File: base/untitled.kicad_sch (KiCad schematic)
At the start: 56 parts, among them U23 6N137, U24 6N137, U25 6N137, U26 6N137, U27 6N137, U28 6N137, U29 6N137, U30 6N137, U31 6N137, U32 6N137, U33 6N137, U34 6N137, U36 6N137, U37 6N137

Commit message: changes to schematic
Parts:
- removed C20, C21, C22, C23, C24, C25, C26, C27, C28, C29, C30, C31, C35, C36: 0.1µ, symbol Device:C
- removed R46, R47, R48, R49, R54, R55, R56, R57, R62, R63, R64, R65, R71, R72: R, symbol Device:R
- removed R50, R51, R52, R53, R58, R59, R60, R61, R66, R67, R68, R69, R73, R74: 330, symbol Device:R
- removed U23, U24, U25, U26, U27, U28, U29, U30, U31, U32, U33, U34, U36, U37: 6N137, Package_DIP:DIP-8_W7.62mm, symbol Isolator:6N137
- added BNO1, STMFuse1, STMFuse2: Polyfuse, Fuse:Fuse_0603_1608Metric_Pad1.05x0.95mm_HandSolder, symbol Device:Polyfuse
- added BNOLED1, MainLED1: LED, LED_SMD:LED_0201_0603Metric, symbol Device:LED
- added J1: MAIN KILL SWITCH, Connector_AMASS:AMASS_XT60-M_1x02_P7.20mm_Vertical, symbol XT60-M:XT60-M
- added J10: ARM KILL SWITCH, Connector_AMASS:AMASS_XT60-M_1x02_P7.20mm_Vertical, symbol XT60-M:XT60-M
- added J11: ISOLATED BUCK IN, Connector_AMASS:AMASS_XT60-M_1x02_P7.20mm_Vertical, symbol XT60-M:XT60-M
- added J12: ISOLATED BUCK OUT, Connector_AMASS:AMASS_XT60-M_1x02_P7.20mm_Vertical, symbol XT60-M:XT60-M
- added J13: JETSON BUCK IN, Connector_AMASS:AMASS_XT60-M_1x02_P7.20mm_Vertical, symbol XT60-M:XT60-M
- added J14: JETSON BUCK OUT, Connector_AMASS:AMASS_XT60-M_1x02_P7.20mm_Vertical, symbol XT60-M:XT60-M
- added J15: JETSON KILL SWITCH, Connector_AMASS:AMASS_XT60-M_1x02_P7.20mm_Vertical, symbol XT60-M:XT60-M
- added J16: 24V TO 12V BUCK (ARM), Connector_AMASS:AMASS_XT60-M_1x02_P7.20mm_Vertical, symbol XT60-M:XT60-M
- added J17: 24V TO 12V BUCK, Connector_AMASS:AMASS_XT60-M_1x02_P7.20mm_Vertical, symbol XT60-M:XT60-M
- added J18: JETSON POWER, Connector_AMASS:AMASS_XT60-M_1x02_P7.20mm_Vertical, symbol XT60-M:XT60-M
- added J19, J21, J22, J23, J28, J29: 12V_BUCK_PINOUTS_ARM, Connector_AMASS:AMASS_XT60-M_1x02_P7.20mm_Vertical, symbol XT60-M:XT60-M
- added J2: MOTOR 1 PWR, Connector_AMASS:AMASS_XT60-M_1x02_P7.20mm_Vertical, symbol XT60-M:XT60-M
- added J20: BatteryIN, Connector_AMASS:AMASS_XT60-M_1x02_P7.20mm_Vertical, symbol XT60-M:XT60-M
- added J24, J25, J26, J27: STEPPER AND BLDC POWER, Connector_AMASS:AMASS_XT60-M_1x02_P7.20mm_Vertical, symbol XT60-M:XT60-M
- added J3: MOTOR 3 PWR, Connector_AMASS:AMASS_XT60-M_1x02_P7.20mm_Vertical, symbol XT60-M:XT60-M
- added J30: ISOLATED STM POWER, Connector_AMASS:AMASS_XT60-M_1x02_P7.20mm_Vertical, symbol XT60-M:XT60-M
- added J31: STM 2 POWER, Connector_AMASS:AMASS_XT60-M_1x02_P7.20mm_Vertical, symbol XT60-M:XT60-M
- added J4: MOTOR 2 PWR, Connector_AMASS:AMASS_XT60-M_1x02_P7.20mm_Vertical, symbol XT60-M:XT60-M
- added J40: EXTRA 12V PORT, Connector_AMASS:AMASS_XT60-M_1x02_P7.20mm_Vertical, symbol XT60-M:XT60-M
- added J41: EXTRA 5V PORT, Connector_AMASS:AMASS_XT60-M_1x02_P7.20mm_Vertical, symbol XT60-M:XT60-M
- added J42, J43: EXTRA 24V PORT, Connector_AMASS:AMASS_XT60-M_1x02_P7.20mm_Vertical, symbol XT60-M:XT60-M
- added J5: MOTOR 4 PWR, Connector_AMASS:AMASS_XT60-M_1x02_P7.20mm_Vertical, symbol XT60-M:XT60-M
- added J6: MOTOR KILL SWITCH, Connector_AMASS:AMASS_XT60-M_1x02_P7.20mm_Vertical, symbol XT60-M:XT60-M
- added J7: BASE KILL SWITCH, Connector_AMASS:AMASS_XT60-M_1x02_P7.20mm_Vertical, symbol XT60-M:XT60-M
- added J8: BUCK JST OUT, Connector_AMASS:AMASS_XT60-M_1x02_P7.20mm_Vertical, symbol XT60-M:XT60-M
- added J9: BUCK JST IN, Connector_AMASS:AMASS_XT60-M_1x02_P7.20mm_Vertical, symbol XT60-M:XT60-M
- added MainFuse1: Fuse, Fuse:Fuseholder_Littelfuse_445_030_series_5x30mm, symbol Device:Fuse
- added R10, R9: R, PCM_4ms_Resistor:R_0603, symbol Device:R
- added U10, U11, U2, U3, U4: USBLC6-4SC6, Package_TO_SOT_SMD:SOT-23-6, symbol Power_Protection:USBLC6-4SC6
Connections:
- net Encoder1A: now also U3.3 (I/O2)
- net Encoder1B: now also U2.1 (I/O1)
- net Encoder2A: now also U3.4 (I/O3)
- net Encoder2B: now also U3.6 (I/O4)
- net Encoder3A: now also U2.4 (I/O3)
- net Encoder3B: now also U2.6 (I/O4)
- net GND: now also J11.N (NEG), J12.N (NEG), J13.P (POS), J14.N (NEG), J16.N (NEG), J17.N (NEG), J18.N (NEG), J19.N (NEG), J2.N (NEG), J20.N (NEG), J21.N (NEG), J22.N (NEG), J23.N (NEG), J24.N (NEG), J25.N (NEG), J26.N (NEG), J27.N (NEG), J28.N (NEG), J29.N (NEG), J3.N (NEG), J30.N (NEG), J31.N (NEG), J4.N (NEG), J40.N (NEG), J41.N (NEG), J42.P (POS), J43.P (POS), J5.N (NEG), J8.P (POS), J9.N (NEG), MainLED1.1 (K), U10.2 (GND), U11.2 (GND), U2.2 (GND), U3.2 (GND)
- net GND1: now also BNOLED1.1 (K), U4.2 (GND)
- net MDD1DIR: now also U11.3 (I/O2)
- net MDD1PWM: now also U11.1 (I/O1)
- net MDD2DIR: now also U10.3 (I/O2)
- net MDD2PWM: now also U10.1 (I/O1)
- net MDD3DIR: now also U11.6 (I/O4)
- net MDD3PWM: now also U11.4 (I/O3)
- net MDD4DIR: now also U10.6 (I/O4)
- net MDD4PWM: now also U10.4 (I/O3)
- net STM5V_ISO: now also STMFuse2.2
- new net: BNOLED1.2 (A), R10.1
- new net: MainLED1.2 (A), R9.1
- new net 12V: J17.P (POS), J19.P (POS), J21.P (POS), J22.P (POS), J23.P (POS), J28.P (POS), J29.P (POS), J40.P (POS)
- new net 24V: J1.N (NEG), J10.P (POS), J13.N (NEG), J15.P (POS), J42.N (NEG), J43.N (NEG), J6.P (POS), J7.P (POS)
- new net 24V_ARM: J10.N (NEG), J16.P (POS), J24.P (POS), J25.P (POS), J26.P (POS), J27.P (POS)
- new net 24V_BASE: J7.N (NEG), J8.N (NEG)
- new net 24V_BATTERY: J1.P (POS), J20.P (POS), MainFuse1.1
- new net 24V_BATTERY_FUSE_IN: MainFuse1.2
- new net 24V_JETSON: J14.P (POS), J15.N (NEG), J18.P (POS)
- new net 24V_MOTOR: J2.P (POS), J3.P (POS), J4.P (POS), J5.P (POS), J6.N (NEG)
- new net 5V: J11.P (POS), J31.P (POS), J41.P (POS), J9.P (POS), R9.2, U10.5 (VBUS), U11.5 (VBUS), U2.5 (VBUS), U3.5 (VBUS)
- new net 5V_ISO: BNO1.2, J12.P (POS), J30.P (POS), STMFuse1.2, U4.5 (VBUS)
- new net 5V_ISO_BNO: BNO1.1, R10.2
- new net 5V_ISO_FUSE_OUT: STMFuse1.1
- new net BNO_SCL: U4.3 (I/O2)
- new net BNO_SDA: U4.1 (I/O1)
- new net STM5V_ISO_IN: STMFuse2.1
- no-connect marks 39 -> 0
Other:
- note added: "12V FOR ARM PCB (SERVO)"
- note added: "24V TO 12 V BUCK ARM"
- note added: "24V TO 5V BUCK"
- note added: "5V TO 5V ISOLATED BUCK"
- note added: "BUCKS"
- note added: "COOLING SYSTEM"
- note added: "EXTRA PORTS"
- note added: "JETSON ISOLATED BUCK"
- note added: "JETSON POWER"
- note added: "KILL SWITCHES"
- note added: "MAIN 24V BATTERY"
- note added: "MOTOR POWER"
- note added: "STEPPER AND BLDC POWER"
- note added: "STM POWER"
- note added: "TVS DIODE"

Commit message: changed the whole schematic and organised it
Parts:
- R10, R9: symbol Device:R -> Device:R_Small_US
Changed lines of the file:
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@@
 	(wire
 		(pts
+			(xy 253.365 125.095) (xy 254.635 125.095)
+		)
+		(stroke
+			(width 0)
+			(type default)
+		)
+	)
+	(wire
+		(pts
 			(xy 19.685 156.845) (xy 19.685 154.94)
 		)
@@
 	(wire
 		(pts
+			(xy 221.615 125.095) (xy 224.155 125.095)
+		)
+		(stroke
+			(width 0)
+			(type default)
+		)
+	)
+	(wire
+		(pts
 			(xy 88.773 188.341) (xy 86.233 188.341)
 		)
@@
 	(wire
 		(pts
-			(xy 107.823 34.163) (xy 107.823 33.528)
+			(xy 215.265 125.095) (xy 216.535 125.095)
 		)
 		(stroke
@@
 	(wire
 		(pts
-			(xy 222.885 125.095) (xy 224.155 125.095)
+			(xy 107.823 34.163) (xy 107.823 33.528)
 		)
 		(stroke
@@
 	(wire
 		(pts
+			(xy 247.015 125.095) (xy 248.285 125.095)
+		)
+		(stroke
+			(width 0)
+			(type default)
+		)
+	)
+	(wire
+		(pts
 			(xy 27.813 90.424) (xy 25.273 90.424)
 		)
@@
 	)
 	(symbol
-		(lib_id "Device:R")
+		(lib_id "Device:R_Small_US")
 		(at 219.075 125.095 90)
 		(unit 1)
@@
 		(fields_autoplaced yes)
 		(property "Reference" "R9"
-			(at 219.075 118.745 90)
+			(at 219.075 119.38 90)
 			(effects
 				(font
@@
 		)
 		(property "Value" "R"
-			(at 219.075 121.285 90)
+			(at 219.075 121.92 90)
 			(effects
 				(font
@@
 		)
 		(property "Footprint" "PCM_4ms_Resistor:R_0603"
-			(at 219.075 126.873 90)
+			(at 219.075 125.095 0)
 			(effects
 				(font
@@
 			)
 		)
-		(property "Description" "Resistor"
+		(property "Description" "Resistor, small US symbol"
 			(at 219.075 125.095 0)
 			(effects
@@
 	)
 	(symbol
-		(lib_id "Device:R")
+		(lib_id "Device:R_Small_US")
 		(at 250.825 125.095 90)
 		(unit 1)
@@
 		(fields_autoplaced yes)
 		(property "Reference" "R10"
-			(at 250.825 118.745 90)
+			(at 250.825 119.38 90)
 			(effects
 				(font
@@
 		)
 		(property "Value" "R"
-			(at 250.825 121.285 90)
+			(at 250.825 121.92 90)
 			(effects
 				(font
@@
 		)
 		(property "Footprint" "PCM_4ms_Resistor:R_0603"
-			(at 250.825 126.873 90)
+			(at 250.825 125.095 0)
 			(effects
 				(font
@@
 			)
 		)
-		(property "Description" "Resistor"
+		(property "Description" "Resistor, small US symbol"
 			(at 250.825 125.095 0)
 			(effects

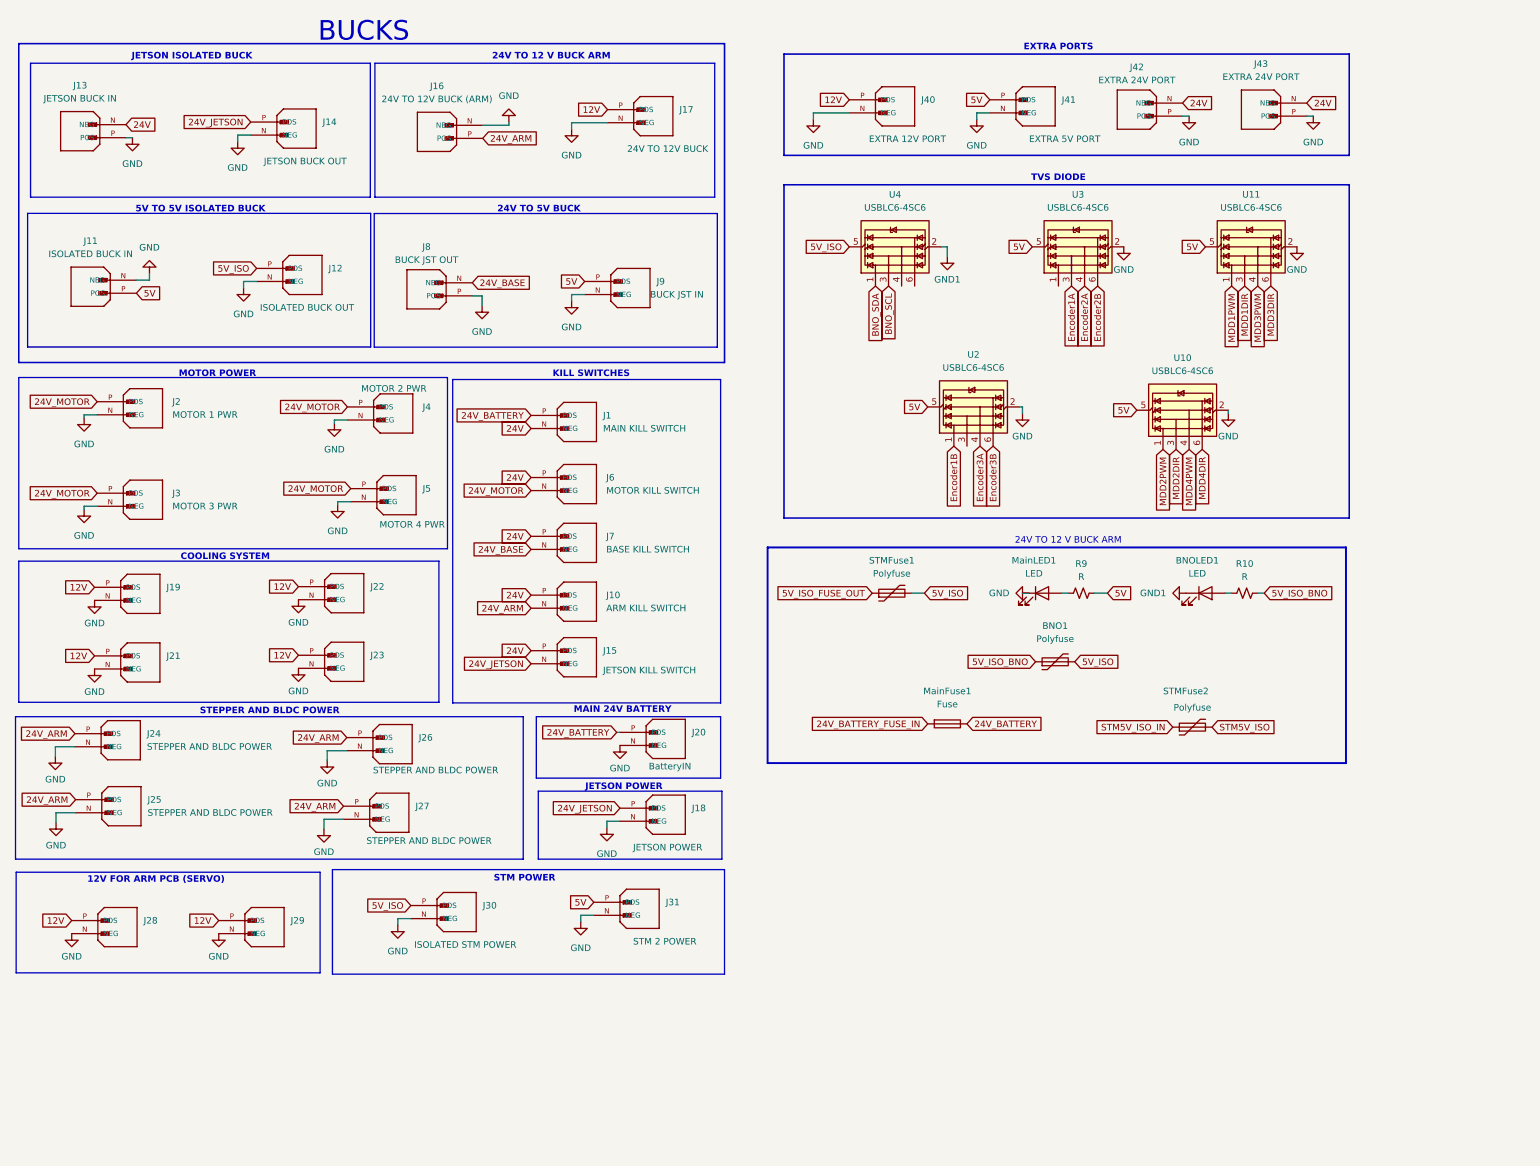
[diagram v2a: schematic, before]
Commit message: components placed\
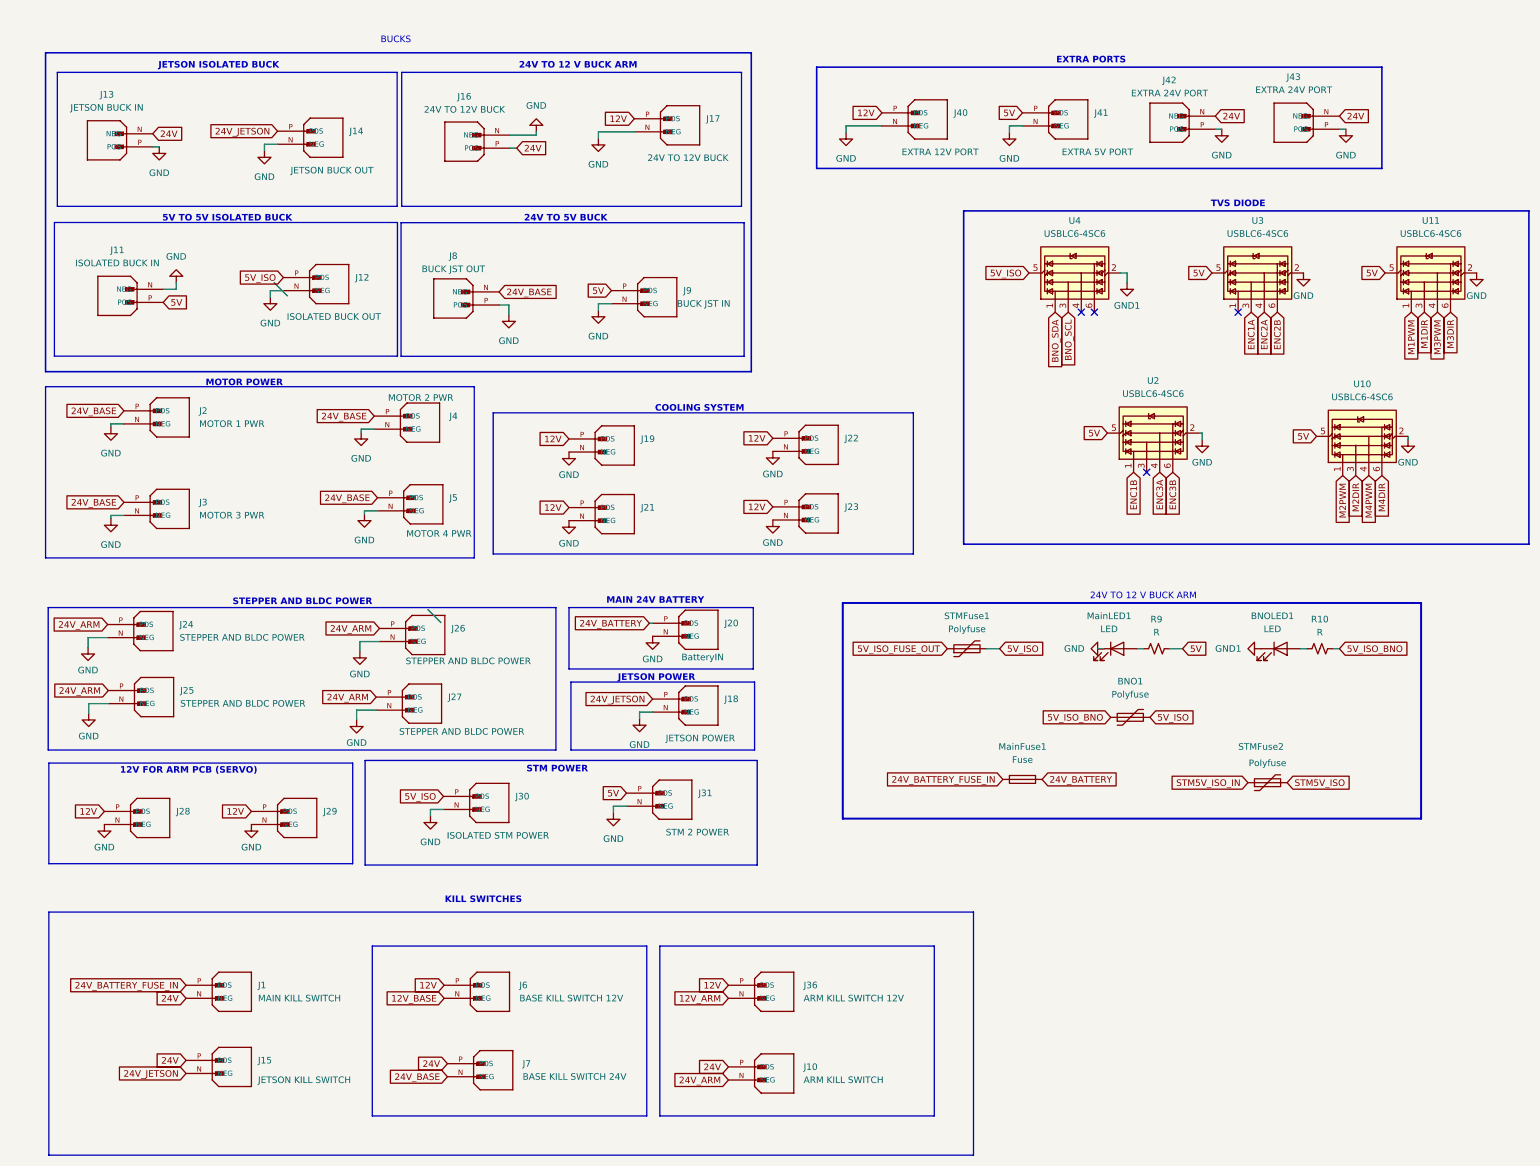
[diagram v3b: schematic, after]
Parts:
- added J36: ARM KILL SWITCH 12V, Connector_AMASS:AMASS_XT60-M_1x02_P7.20mm_Vertical, symbol XT60-M:XT60-M
- J16: value 24V TO 12V BUCK (ARM) -> 24V TO 12V BUCK
- J6: value MOTOR KILL SWITCH -> BASE KILL SWITCH 12V
- J7: value BASE KILL SWITCH -> BASE KILL SWITCH 24V
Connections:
- net 12V: now also J6.P (POS), J36.P (POS)
- net 24V: now also J16.P (POS); no longer J6.P (POS)
- net 24V_ARM: no longer J16.P (POS)
- net 24V_BASE: now also J2.P (POS), J3.P (POS), J4.P (POS), J5.P (POS)
- net 24V_BATTERY: no longer J1.P (POS)
- net 24V_BATTERY_FUSE_IN: now also J1.P (POS)
- removed net 24V_MOTOR: J2.P (POS), J3.P (POS), J4.P (POS), J5.P (POS), J6.N (NEG)
- net Encoder1A renamed ENC1A
- net Encoder1B renamed ENC1B
- net Encoder2A renamed ENC2A
- net Encoder2B renamed ENC2B
- net Encoder3A renamed ENC3A
- net Encoder3B renamed ENC3B
- net MDD1DIR renamed M1DIR
- net MDD1PWM renamed M1PWM
- net MDD2DIR renamed M2DIR
- net MDD2PWM renamed M2PWM
- net MDD3DIR renamed M3DIR
- net MDD3PWM renamed M3PWM
- net MDD4DIR renamed M4DIR
- net MDD4PWM renamed M4PWM
- new net 12V_ARM: J36.N (NEG)
- new net 12V_BASE: J6.N (NEG)
- no-connect marks 0 -> 4
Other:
- moved on the sheet: BNO1, BNOLED1, J1, J10, J11, J12, J13, J14, J15, J16, J17, J18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

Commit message: made the suggested changes
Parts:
- removed BNOLED1, MainLED1: LED, LED_SMD:LED_0201_0603Metric, symbol Device:LED
- removed J11: ISOLATED BUCK IN, Connector_AMASS:AMASS_XT60-M_1x02_P7.20mm_Vertical, symbol XT60-M:XT60-M
- removed J12: ISOLATED BUCK OUT, Connector_AMASS:AMASS_XT60-M_1x02_P7.20mm_Vertical, symbol XT60-M:XT60-M
- removed J13: JETSON BUCK IN, Connector_AMASS:AMASS_XT60-M_1x02_P7.20mm_Vertical, symbol XT60-M:XT60-M
- removed J14: JETSON BUCK OUT, Connector_AMASS:AMASS_XT60-M_1x02_P7.20mm_Vertical, symbol XT60-M:XT60-M
- removed J25, J26, J27: STEPPER AND BLDC POWER, Connector_AMASS:AMASS_XT60-M_1x02_P7.20mm_Vertical, symbol XT60-M:XT60-M
- removed J30: ISOLATED STM POWER, Connector_AMASS:AMASS_XT60-M_1x02_P7.20mm_Vertical, symbol XT60-M:XT60-M
- removed J31: STM 2 POWER, Connector_AMASS:AMASS_XT60-M_1x02_P7.20mm_Vertical, symbol XT60-M:XT60-M
- removed J43: EXTRA 24V PORT, Connector_AMASS:AMASS_XT60-M_1x02_P7.20mm_Vertical, symbol XT60-M:XT60-M
- removed MainFuse1: Fuse, Fuse:Fuseholder_Littelfuse_445_030_series_5x30mm, symbol Device:Fuse
- removed R10, R9: R, PCM_4ms_Resistor:R_0603, symbol Device:R_Small_US
- J28, J29: footprint Connector_AMASS:AMASS_XT60-M_1x02_P7.20mm_Vertical -> Connector_JST:JST_XH_B2B-XH-A_1x02_P2.50mm_Vertical
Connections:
- net 24V_BATTERY_FUSE_IN is gone; now on net 24V_BATTERY: J1.P (POS)
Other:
- note added: "24V TO 12 V BUCK"
- note removed: "5V TO 5V ISOLATED BUCK"
- note removed: "JETSON ISOLATED BUCK"
- note removed: "STM POWER"
- moved on the sheet: BNO1, J18, J20, J24, J28, J29, STMFuse1, STMFuse2

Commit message: 50% routing done
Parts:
- removed J15: JETSON KILL SWITCH, Connector_AMASS:AMASS_XT60-M_1x02_P7.20mm_Vertical, symbol XT60-M:XT60-M
- removed J28, J29: 12V_BUCK_PINOUTS_ARM, Connector_JST:JST_XH_B2B-XH-A_1x02_P2.50mm_Vertical, symbol XT60-M:XT60-M
- added H5, H6, H7, H8: MountingHole_Pad, MountingHole:MountingHole_4.3mm_M4_DIN965_Pad_TopBottom, symbol Mechanical:MountingHole_Pad
- added J30: Conn_01x03_Pin, Connector_JST:JST_XH_B3B-XH-A_1x03_P2.50mm_Vertical, symbol Connector:Conn_01x03_Pin
- added J31: Conn_01x03_Pin, Connector_JST:JST_XH_B3B-XH-AM_1x03_P2.50mm_Vertical, symbol Connector:Conn_01x03_Pin
- J10: renamed from J1; footprint Connector_AMASS:AMASS_XT60-M_1x02_P7.20mm_Vertical -> ROBO:xt60
- J11: renamed from J20; footprint Connector_AMASS:AMASS_XT60-M_1x02_P7.20mm_Vertical -> ROBO:xt60
- J13: renamed from J4; footprint Connector_AMASS:AMASS_XT60-M_1x02_P7.20mm_Vertical -> ROBO:xt60
- J14: renamed from J5; footprint Connector_AMASS:AMASS_XT60-M_1x02_P7.20mm_Vertical -> ROBO:xt60
- J15: renamed from J8; value BUCK JST OUT -> 24V TO 5V BUCK IN; footprint Connector_AMASS:AMASS_XT60-M_1x02_P7.20mm_Vertical -> ROBO:xt60
- J16: renamed from J6; footprint Connector_AMASS:AMASS_XT60-M_1x02_P7.20mm_Vertical -> ROBO:xt60
- J17: renamed from J7; footprint Connector_AMASS:AMASS_XT60-M_1x02_P7.20mm_Vertical -> ROBO:xt60
- J18: renamed from J16; value 24V TO 12V BUCK -> 24V TO 12V BUCK IN; footprint Connector_AMASS:AMASS_XT60-M_1x02_P7.20mm_Vertical -> ROBO:xt60
- J19: value 12V_BUCK_PINOUTS_ARM -> COOLING SYSTEM; footprint Connector_AMASS:AMASS_XT60-M_1x02_P7.20mm_Vertical -> ROBO:xt60
- J20: renamed from J21; value 12V_BUCK_PINOUTS_ARM -> COOLING SYSTEM; footprint Connector_AMASS:AMASS_XT60-M_1x02_P7.20mm_Vertical -> ROBO:xt60
- J21: renamed from J9; value BUCK JST IN -> 24V TO 5V BUCK OUT; footprint Connector_AMASS:AMASS_XT60-M_1x02_P7.20mm_Vertical -> ROBO:xt60
- J22: renamed from J17; value 24V TO 12V BUCK -> 24V TO 12V BUCK OUT; footprint Connector_AMASS:AMASS_XT60-M_1x02_P7.20mm_Vertical -> ROBO:xt60
- J23: renamed from J36; footprint Connector_AMASS:AMASS_XT60-M_1x02_P7.20mm_Vertical -> ROBO:xt60
- J24: renamed from J10; footprint Connector_AMASS:AMASS_XT60-M_1x02_P7.20mm_Vertical -> ROBO:xt60
- J25: renamed from J22; value 12V_BUCK_PINOUTS_ARM -> COOLING SYSTEM; footprint Connector_AMASS:AMASS_XT60-M_1x02_P7.20mm_Vertical -> ROBO:xt60
- J26: renamed from J23; value 12V_BUCK_PINOUTS_ARM -> COOLING SYSTEM; footprint Connector_AMASS:AMASS_XT60-M_1x02_P7.20mm_Vertical -> ROBO:xt60
- J27: renamed from J40; footprint Connector_AMASS:AMASS_XT60-M_1x02_P7.20mm_Vertical -> ROBO:xt60
- J28: renamed from J41; footprint Connector_AMASS:AMASS_XT60-M_1x02_P7.20mm_Vertical -> ROBO:xt60
- J29: renamed from J42; footprint Connector_AMASS:AMASS_XT60-M_1x02_P7.20mm_Vertical -> ROBO:xt60
- J6: renamed from J2; footprint Connector_AMASS:AMASS_XT60-M_1x02_P7.20mm_Vertical -> ROBO:xt60
- J7: renamed from J3; footprint Connector_AMASS:AMASS_XT60-M_1x02_P7.20mm_Vertical -> ROBO:xt60
- J8: renamed from J24; footprint Connector_AMASS:AMASS_XT60-M_1x02_P7.20mm_Vertical -> ROBO:xt60
- J9: renamed from J18; footprint Connector_AMASS:AMASS_XT60-M_1x02_P7.20mm_Vertical -> ROBO:xt60
- renumbered U2 to U5, U3 to U6, U10 to U7, U11 to U8
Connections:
- net 24V_JETSON is gone; now on net 24V: J9.P (POS)
- net STM5V_ISO_IN is gone; now on net 5V: STMFuse2.1
- net 12V: now also J30.2 (Pin_2), J31.2 (Pin_2)
- net GND: now also J30.1 (Pin_1), J31.1 (Pin_1)
- net STM5V_ISO renamed 5V_NON_ISO_IN
- new net Chassis: H5.1, H6.1, H7.1, H8.1
- no-connect marks 4 -> 6
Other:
- note added: "Mounting Holes"
- moved on the sheet: BNO1, J10, J11, J16, J17, J23, J24, STMFuse1, STMFuse2

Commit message: 1st iteration complete
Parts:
- J31: footprint Connector_JST:JST_XH_B3B-XH-AM_1x03_P2.50mm_Vertical -> Connector_JST:JST_XH_B3B-XH-A_1x03_P2.50mm_Vertical
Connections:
- net 12V: no longer J30.2 (Pin_2), J31.2 (Pin_2)
- net 12V_ARM: now also J30.2 (Pin_2), J31.2 (Pin_2)
- net 24V: now also J29.P (POS); no longer J29.N (NEG)
- net 24V_BASE: now also J15.P (POS); no longer J15.N (NEG)
- net GND: now also J15.N (NEG), J29.N (NEG); no longer J15.P (POS), J29.P (POS)
